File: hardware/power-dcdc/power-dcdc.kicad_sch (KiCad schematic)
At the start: 69 parts, among them J1 SOLAR_IN, J2 DCDC-MEASURES, J3 DCDC-PWM, J4 BATT2, J5 BATT1, Q1 SIR164ADP, Q2 SIR164ADP, Q3 SI7149ADP, Q4 SI7149ADP, Q5 SI7149ADP, Q6 SI7149ADP, U1 LP4951C, U2 NCP5901B, U3 PAC1953-1, U4 DGD0215, U5 DGD0215

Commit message: One more P/N update
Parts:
- C2: P/N C1206C104K5RACTU -> C1206C104K5RACTU (M)
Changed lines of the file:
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@@
       (effects (font (size 1.27 1.27)) hide)
     )
-    (property "P/N" "C1206C104K5RACTU" (id 4) (at 72.39 35.56 0)
+    (property "P/N" "C1206C104K5RACTU (M)" (id 4) (at 72.39 35.56 0)
       (effects (font (size 1.27 1.27)) hide)
     )

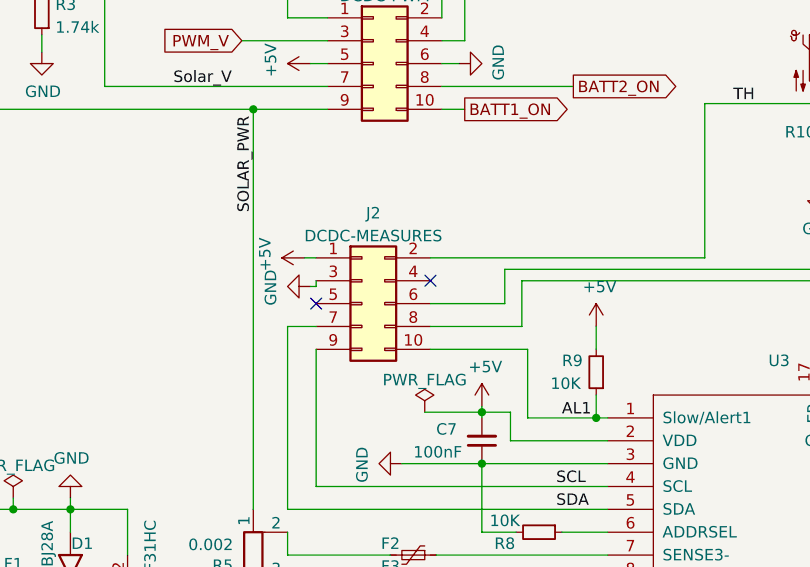
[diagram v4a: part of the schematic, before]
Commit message: *: connect unused connectors pins to GND
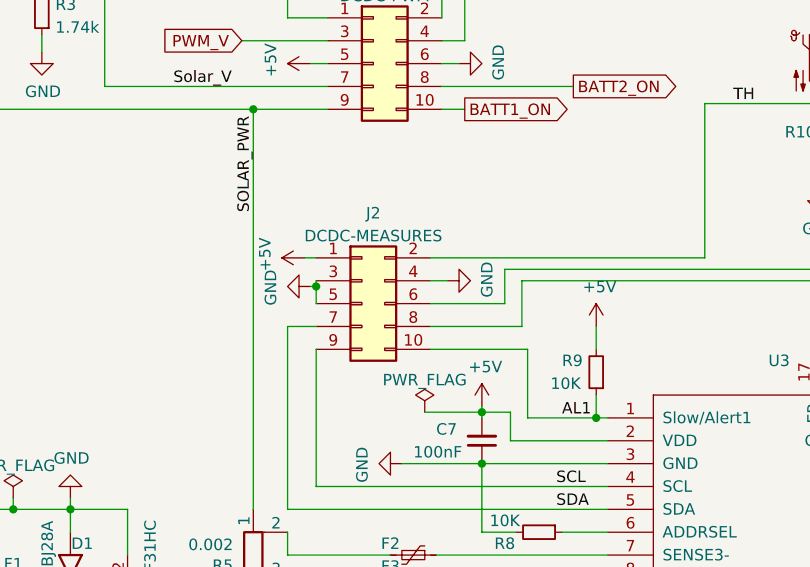
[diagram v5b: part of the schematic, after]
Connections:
- net GND: now also J2.4 (Pin_4), J2.5 (Pin_5)
- no-connect marks 4 -> 2
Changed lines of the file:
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@@
   (junction (at 236.22 97.79) (diameter 0) (color 0 0 0 0)
   )
+  (junction (at 86.995 114.935) (diameter 0) (color 0 0 0 0)
+  )
   (junction (at 255.27 118.11) (diameter 0) (color 0 0 0 0)
   )
@@
   (junction (at 162.56 73.66) (diameter 0) (color 0 0 0 0)
   )
-  (no_connect (at 86.995 116.84))
-  (no_connect (at 99.695 114.3))
   (no_connect (at 66.04 59.69))
   (no_connect (at 93.98 57.15))
@@
     (stroke (width 0) (type default) (color 0 0 0 0))
   )
+  (wire (pts (xy 86.995 114.935) (xy 86.995 116.84))
+    (stroke (width 0) (type default) (color 0 0 0 0))
+  )
   (wire (pts (xy 196.85 58.42) (xy 196.85 62.23))
     (stroke (width 0) (type default) (color 0 0 0 0))
@@
   )
   (wire (pts (xy 229.87 106.68) (xy 227.33 106.68))
+    (stroke (width 0) (type default) (color 0 0 0 0))
+  )
+  (wire (pts (xy 99.695 114.3) (xy 101.6 114.3))
     (stroke (width 0) (type default) (color 0 0 0 0))
   )
@@
     )
     (property "Datasheet" "" (id 3) (at 158.75 119.38 0)
+      (effects (font (size 1.27 1.27)) hide)
+    )
+    (pin "1")
+  )
+  (symbol (lib_id "power:GND") (at 101.6 114.3 90) (unit 1)
+    (in_bom yes) (on_board yes)
+    (property "Reference" "#PWR?" (id 0) (at 107.95 114.3 0)
+      (effects (font (size 1.27 1.27)) hide)
+    )
+    (property "Value" "GND" (id 1) (at 105.9942 114.173 0))
+    (property "Footprint" "" (id 2) (at 101.6 114.3 0)
+      (effects (font (size 1.27 1.27)) hide)
+    )
+    (property "Datasheet" "" (id 3) (at 101.6 114.3 0)
       (effects (font (size 1.27 1.27)) hide)
     )
@@
       (reference "#PWR024") (unit 1) (value "GND") (footprint "")
     )
+    (path "/4048d801-a6f5-4b3d-8bcd-751185512828"
+      (reference "#PWR?") (unit 1) (value "GND") (footprint "")
+    )
     (path "/e2f6369a-02b5-4d5b-ba47-235a0926e866"

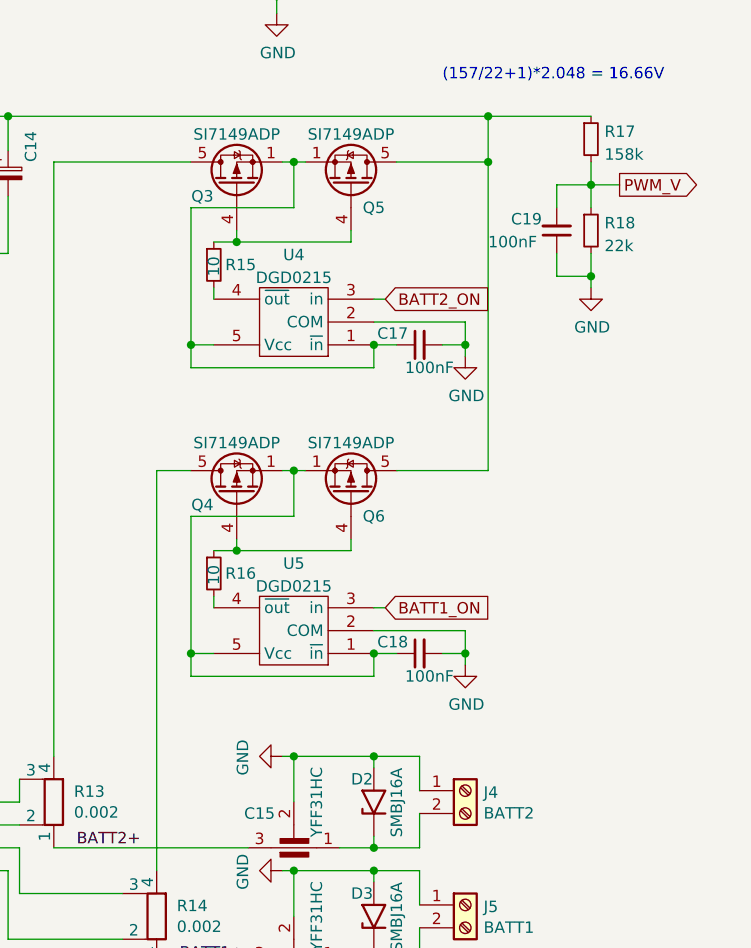
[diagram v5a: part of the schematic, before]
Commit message: Tests have shown that the DGD0215 behavior when driven while not powered is quite bad: not only the drive voltage is forwarded to its Vcc pin (this is expexted), but when the voltage rises on Vcc this higher voltage is feed back to the in pin. Although it's not supposed to happen in normal use, protect from this by introducing a pullup+mosfet in the control path to isolate it from the power part a bit more. While there add dischage resistors to the power mosfet gates.
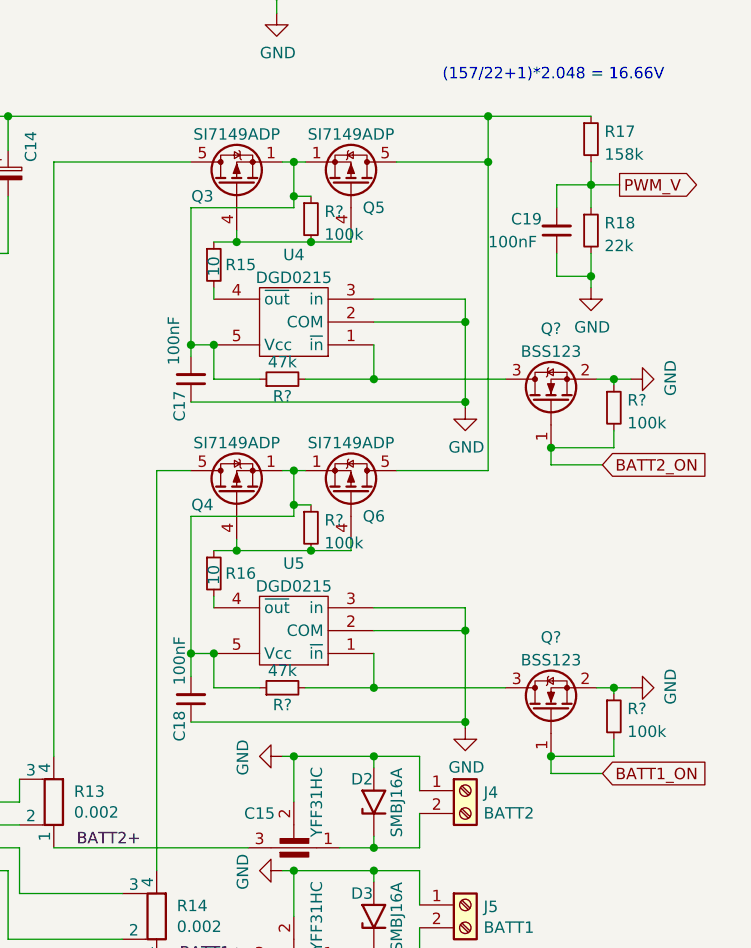
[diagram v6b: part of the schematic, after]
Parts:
- added Q? (x2): BSS123, Package_TO_SOT_SMD:SOT-23, symbol Device:Q_NMOS_GSD
- added R? (x4): 100k, Resistor_SMD:R_0805_2012Metric_Pad1.20x1.40mm_HandSolder, symbol Device:R_Small
- added R? (x2): 47k, Resistor_SMD:R_0805_2012Metric_Pad1.20x1.40mm_HandSolder, symbol Device:R_Small
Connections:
- net BATT1_ON: now also Q?.1 (G), R?.2; no longer U5.3 (in)
- net BATT2_ON: now also Q?.1 (G), R?.2; no longer U4.3 (in)
- net GND: now also C17.1, C18.1, U4.3 (in), U5.3 (in), Q?.2 (S), Q?.2 (S), R?.1, R?.1; no longer C17.2, C18.2
- net at Q3.1 (S), Q3.2 (S), Q3.3 (S)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: now also C17.2, R?.1, R?.1; no longer C17.1, U4.1 (~{in})
- net at Q3.4 (G), Q5.4 (G), R15.1: now also R?.2
- net at Q4.1 (S), Q4.2 (S), Q4.3 (S)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: now also C18.2, R?.1, R?.1; no longer C18.1, U5.1 (~{in})
- net at Q4.4 (G), Q6.4 (G), R16.1: now also R?.2
- new net: Q?.3 (D), R?.2, U4.1 (~{in})
- new net: Q?.3 (D), R?.2, U5.1 (~{in})
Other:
- moved on the sheet: C17, C18

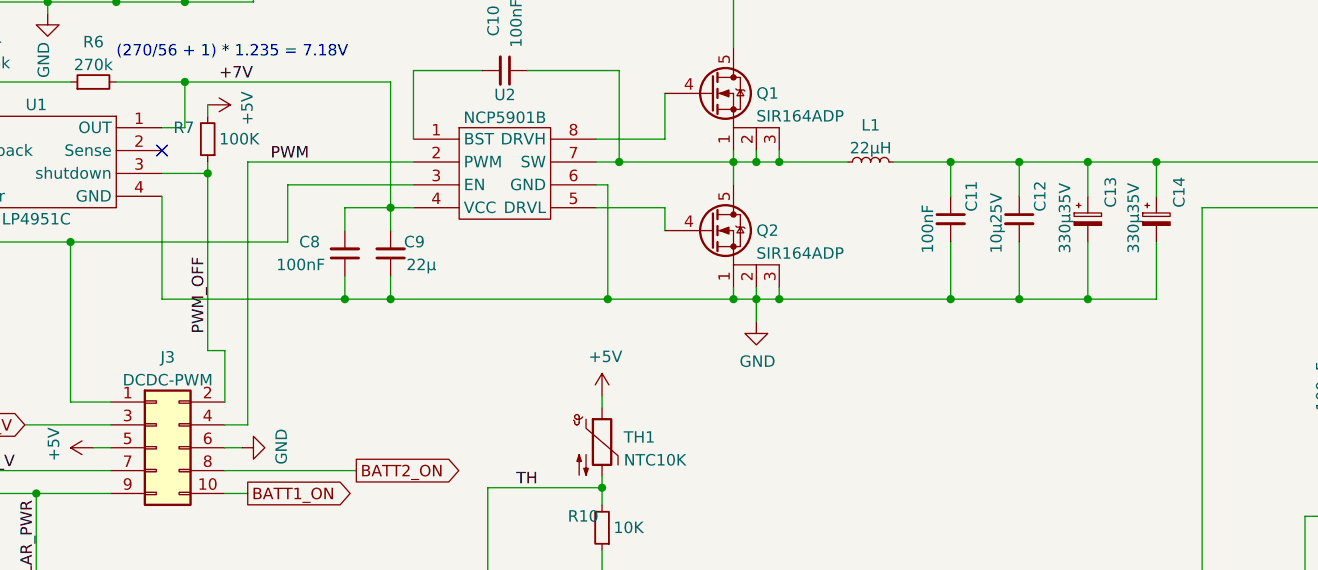
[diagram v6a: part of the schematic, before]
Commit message: power-dcdc: testings have shown that the NCP5901 zero cross detection trips way too early, leaving most of the low side current trough the body diode of the mosfet. It starts working properly at 3A. This is because the mosfet's Rdson is too low (!). Finding a mosfet with a proper Rdson while keeping the same performance, and in an easy-to-use package isn't that easy. So use resistors instead to increase the voltage across the low-side transistor. With 2 20mOhms resistors in parallel ZCD should start working properly between 0.5 and 0.6A.
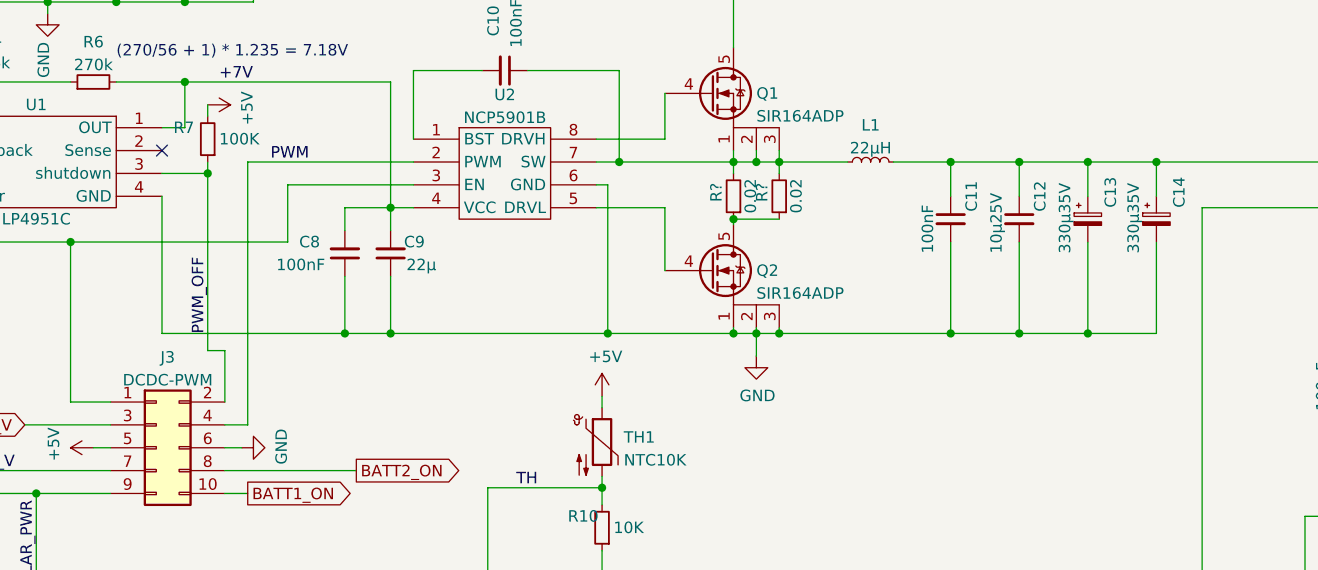
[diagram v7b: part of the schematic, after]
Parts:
- added R? (x2): 0.02, Resistor_SMD:R_2010_5025Metric_Pad1.40x2.65mm_HandSolder, symbol Device:R_Small
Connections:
- net PWM_OFF is gone; now on net GND: J3.2 (Pin_2), R7.1, U1.3 (shutdown)
- net at C10.1, L1.1, Q1.1 (S)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: now also R?.2, R?.2; no longer Q2.5 (D)
- new net: Q2.5 (D), R?.1, R?.1
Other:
- moved on the sheet: Q2

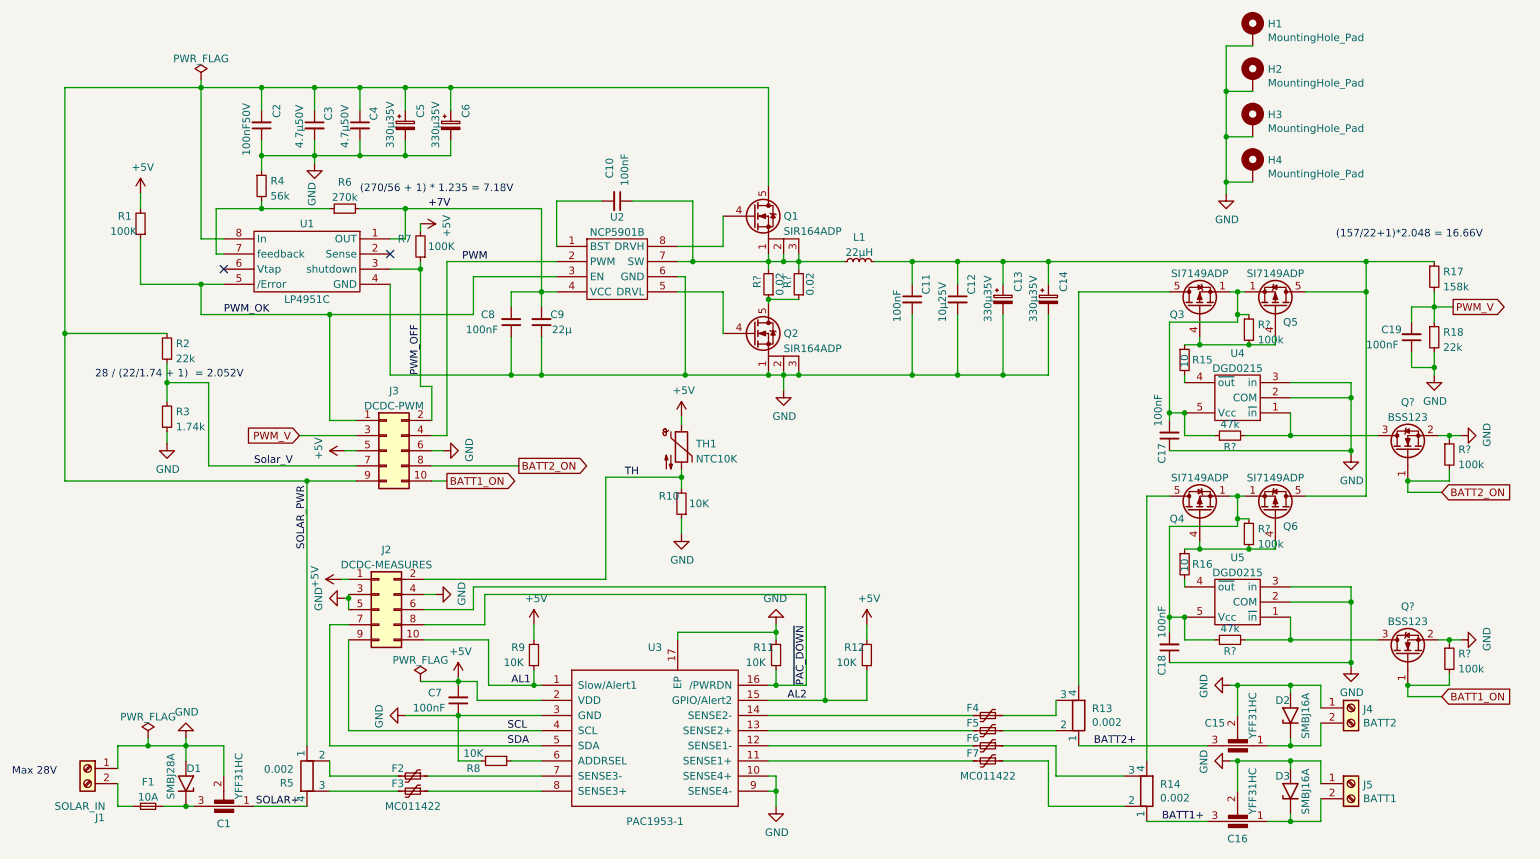
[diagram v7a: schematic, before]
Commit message: Re-anotate schematic (from scratch)
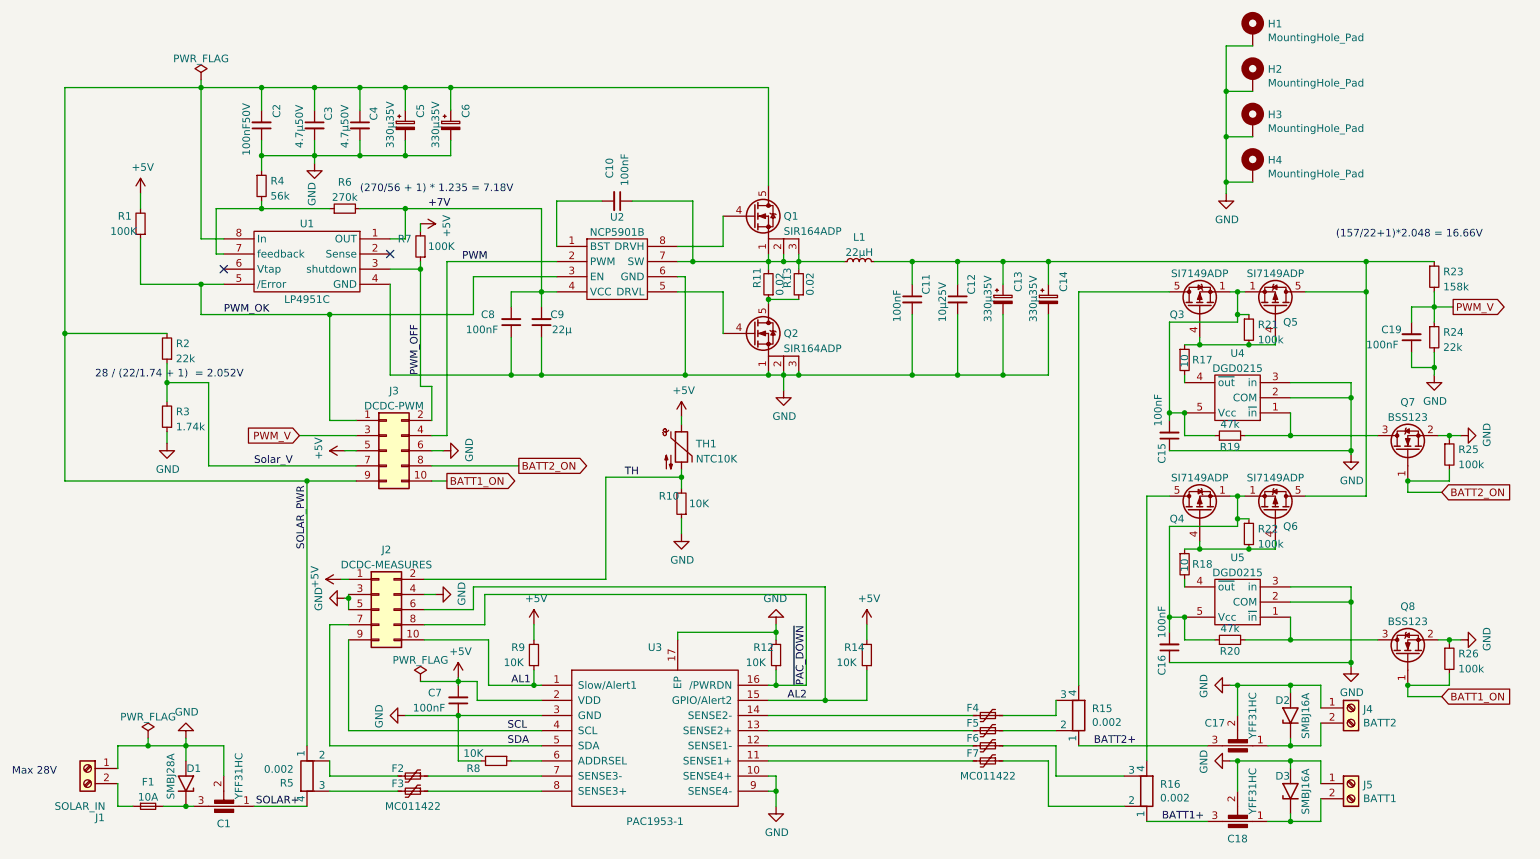
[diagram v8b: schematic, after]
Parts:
- gave numbers to parts that had none: 10
- renumbered C17 to C15, C18 to C16, C15 to C17, C16 to C18, R11 to R12, R12 to R14, R13 to R15, R14 to R16, R15 to R17, R16 to R18, R17 to R23, R18 to R24
